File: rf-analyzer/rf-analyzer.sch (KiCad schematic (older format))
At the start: 57 parts, among them U1 AD8302, U2 AD8302

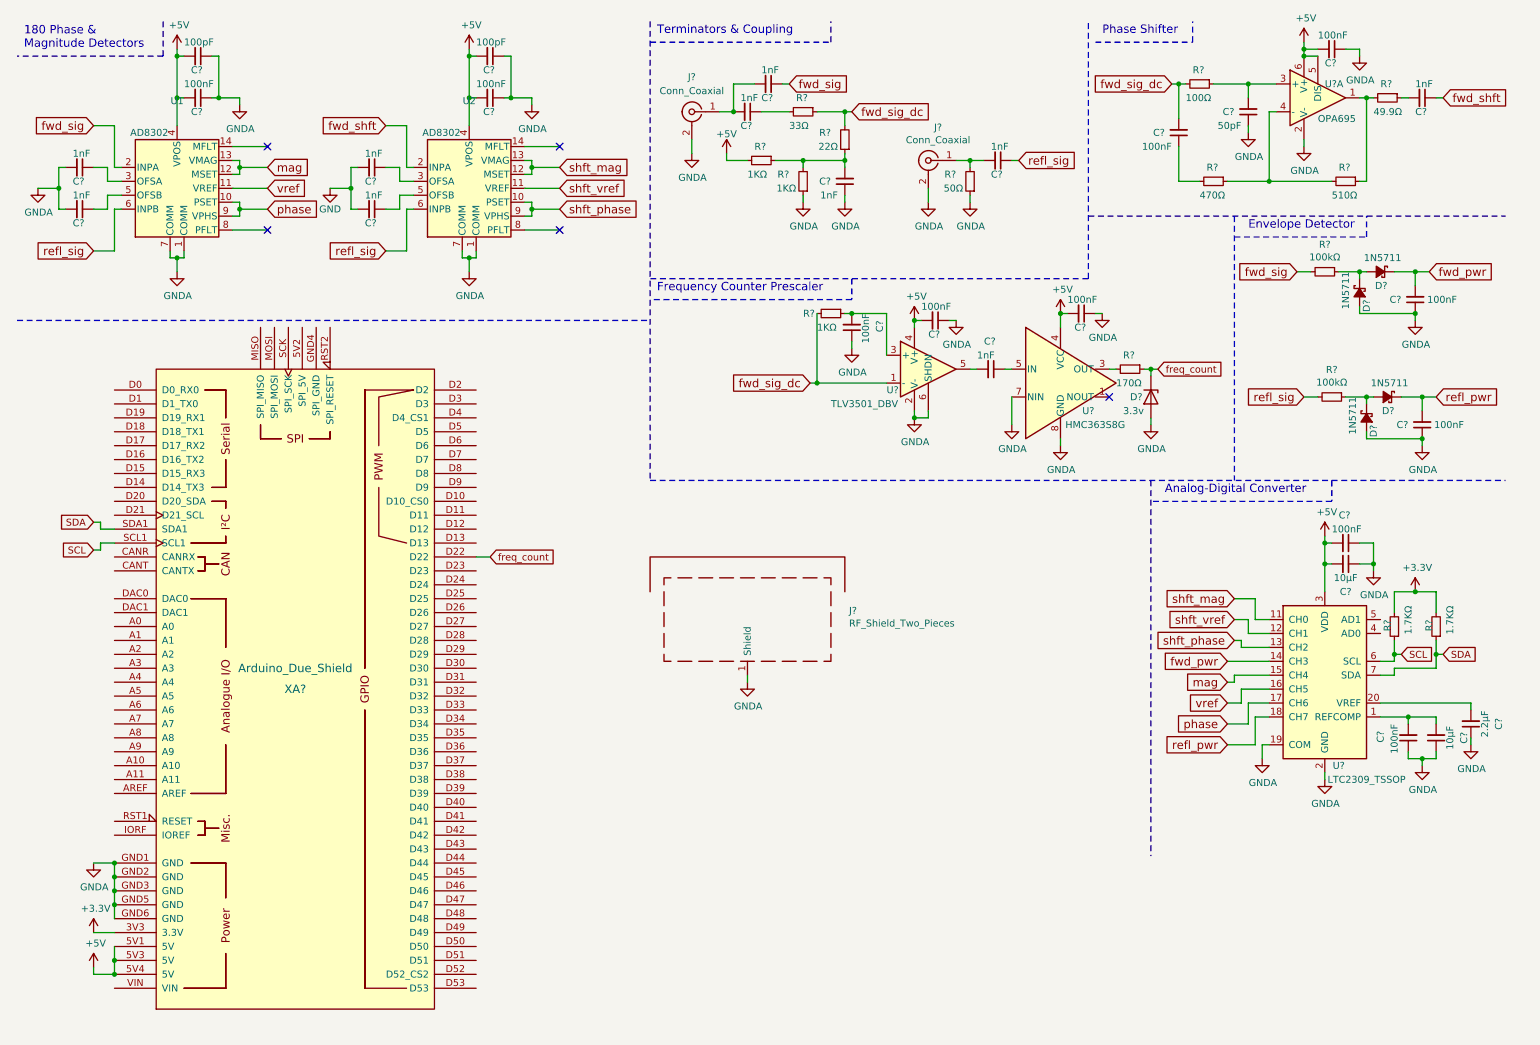
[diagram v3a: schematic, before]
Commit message: moved tank on powerrail to new location.
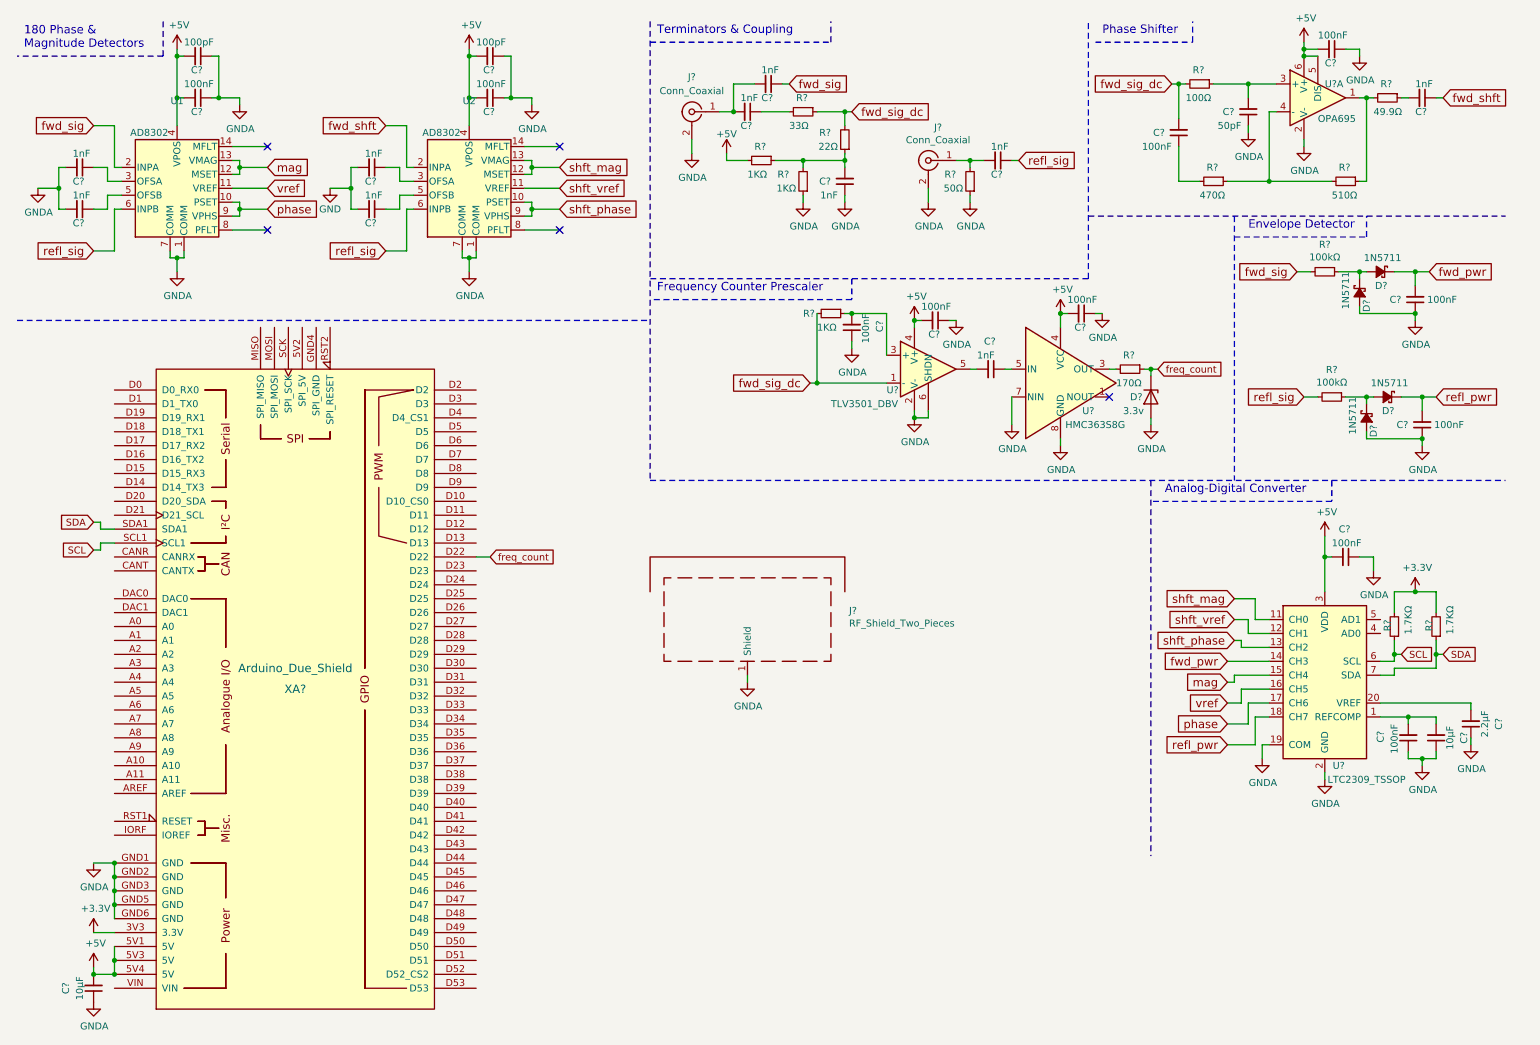
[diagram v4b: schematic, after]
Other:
- moved on the sheet: C?
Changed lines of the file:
@@
 L Device:C_Small C?
 U 1 1 5C8820EC
-P 10050 4250
-F 0 "C?" V 9850 4200 50  0000 L CNN
-F 1 "100nF" V 9950 4150 50  0000 L CNN
-F 2 "Capacitor_SMD:C_0603_1608Metric_Pad1.05x0.95mm_HandSolder" H 10050 4250 50  0001 C CNN
-F 3 "" H 10050 4250 50  0001 C CNN
-	1    10050 4250
+P 10050 4350
+F 0 "C?" V 9850 4300 50  0000 L CNN
+F 1 "100nF" V 9950 4250 50  0000 L CNN
+F 2 "Capacitor_SMD:C_0603_1608Metric_Pad1.05x0.95mm_HandSolder" H 10050 4350 50  0001 C CNN
+F 3 "" H 10050 4350 50  0001 C CNN
+	1    10050 4350
 	0    1    1    0
 $EndComp
@@
 L Device:C_Small C?
 U 1 1 5C882A0E
-P 10050 4400
-F 0 "C?" V 10250 4400 50  0000 C CNN
-F 1 "10μF" V 10150 4400 50  0000 C CNN
-F 2 "" H 10050 4400 50  0001 C CNN
-F 3 "~" H 10050 4400 50  0001 C CNN
-	1    10050 4400
-	0    1    1    0
+P 1050 7450
+F 0 "C?" V 1250 7450 50  0000 C CNN
+F 1 "10μF" V 1150 7450 50  0000 C CNN
+F 2 "" H 1050 7450 50  0001 C CNN
+F 3 "~" H 1050 7450 50  0001 C CNN
+	1    1050 7450
+	-1   0    0    1
 $EndComp
 $Comp
@@
 $EndComp
 Wire Wire Line
-	9900 4600 9900 4400
-Wire Wire Line
-	9900 4250 9950 4250
-Wire Wire Line
-	9950 4400 9900 4400
-Connection ~ 9900 4400
-Wire Wire Line
-	9900 4400 9900 4250
-Wire Wire Line
-	10250 4450 10250 4400
-Wire Wire Line
-	10250 4250 10150 4250
-Wire Wire Line
-	10150 4400 10250 4400
-Connection ~ 10250 4400
-Wire Wire Line
-	10250 4400 10250 4250
+	9900 4350 9950 4350
 $Comp
 L power:+5V #PWR?
@@
 	1    0    0    -1
 $EndComp
-Wire Wire Line
-	9900 4200 9900 4250
-Connection ~ 9900 4250
 $Comp
 L power:GNDA #PWR?
@@
 Wire Wire Line
 	1050 7300 1050 7350
-Wire Wire Line
-	1200 6550 1050 6550
 $Comp
 L arduino:Arduino_Due_Shield XA?
@@
 Wire Notes Line
 	8200 2350 5050 2350
+Wire Wire Line
+	9900 4200 9900 4350
+Connection ~ 9900 4350
+Wire Wire Line
+	9900 4350 9900 4600
+Wire Wire Line
+	10250 4450 10250 4350
+Wire Wire Line
+	10250 4350 10150 4350
+Connection ~ 1050 7350
+Wire Wire Line
+	1050 6550 1200 6550
+$Comp
+L power:GNDA #PWR?
+U 1 1 60478DD4
+P 1050 7550
+F 0 "#PWR?" H 1050 7300 50  0001 C CNN
+F 1 "GNDA" H 1055 7377 50  0000 C CNN
+F 2 "" H 1050 7550 50  0001 C CNN
+F 3 "" H 1050 7550 50  0001 C CNN
+	1    1050 7550
+	1    0    0    -1
+$EndComp
 $EndSCHEMATC

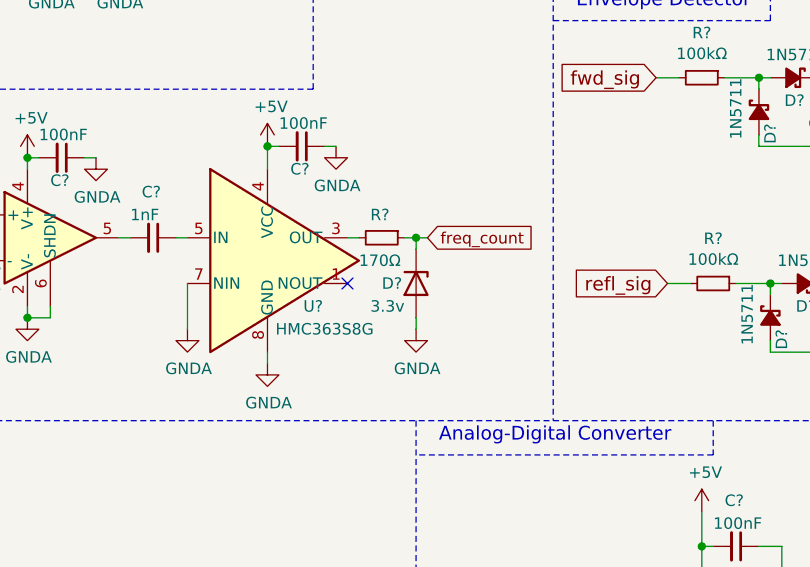
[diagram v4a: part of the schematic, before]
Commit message: Replaced the zener with a voltage divder for better frequency response.
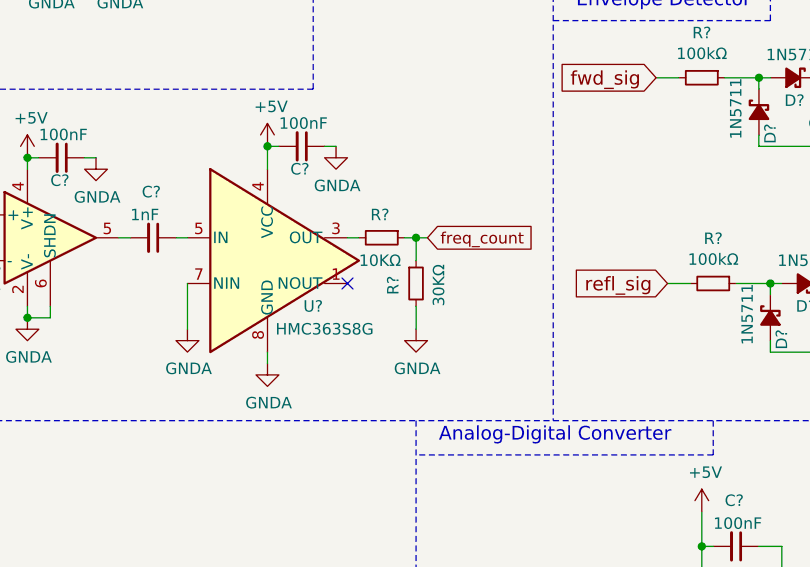
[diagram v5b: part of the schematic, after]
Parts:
- removed D?: 3.3v, symbol Device:D_Zener
- added R?: 30KΩ, Resistor_SMD:R_0603_1608Metric_Pad1.05x0.95mm_HandSolder, symbol Device:R_Small
- R?: value 170Ω -> 10KΩ
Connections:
- net GNDA: now also R?.2
- net freq_count: now also R?.1
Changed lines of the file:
@@
 	6200 3100 6250 3100
-$Comp
-L Device:R_Small R?
-U 1 1 5F77CD96
-P 8500 3000
-F 0 "R?" V 8400 2950 50  0000 L CNN
-F 1 "170Ω" V 8600 2900 50  0000 L CNN
-F 2 "Resistor_SMD:R_0603_1608Metric_Pad1.05x0.95mm_HandSolder" H 8500 3000 50  0001 C CNN
-F 3 "" H 8500 3000 50  0001 C CNN
-	1    8500 3000
-	0    1    1    0
-$EndComp
-$Comp
-L Device:D_Zener D?
-U 1 1 5F7D1F53
-P 8650 3200
-F 0 "D?" V 8650 3050 50  0000 L CNN
-F 1 "3.3v" V 8750 3000 50  0000 L CNN
-F 2 "" H 8650 3200 50  0001 C CNN
-F 3 "~" H 8650 3200 50  0001 C CNN
-	1    8650 3200
-	0    1    1    0
-$EndComp
 $Comp
 L power:GNDA #PWR?
@@
 Wire Wire Line
 	8600 3000 8650 3000
-Wire Wire Line
-	8650 3000 8650 3050
-Wire Wire Line
-	8650 3350 8650 3400
 $Comp
 L power:+5V #PWR?
@@
 	1    0    0    -1
 $EndComp
+$Comp
+L Device:R_Small R?
+U 1 1 5F77CD96
+P 8500 3000
+F 0 "R?" V 8400 2950 50  0000 L CNN
+F 1 "10KΩ" V 8600 2900 50  0000 L CNN
+F 2 "Resistor_SMD:R_0603_1608Metric_Pad1.05x0.95mm_HandSolder" H 8500 3000 50  0001 C CNN
+F 3 "" H 8500 3000 50  0001 C CNN
+	1    8500 3000
+	0    1    1    0
+$EndComp
+$Comp
+L Device:R_Small R?
+U 1 1 604D1349
+P 8650 3200
+F 0 "R?" V 8550 3150 50  0000 L CNN
+F 1 "30KΩ" V 8750 3100 50  0000 L CNN
+F 2 "Resistor_SMD:R_0603_1608Metric_Pad1.05x0.95mm_HandSolder" H 8650 3200 50  0001 C CNN
+F 3 "" H 8650 3200 50  0001 C CNN
+	1    8650 3200
+	1    0    0    -1
+$EndComp
+Wire Wire Line
+	8650 3000 8650 3100
+Wire Wire Line
+	8650 3300 8650 3400
 $EndSCHEMATC

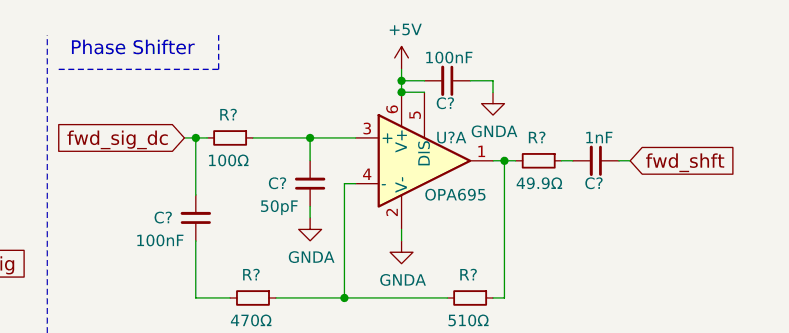
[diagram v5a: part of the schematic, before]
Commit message: moved around a power rail that was outside of the border.
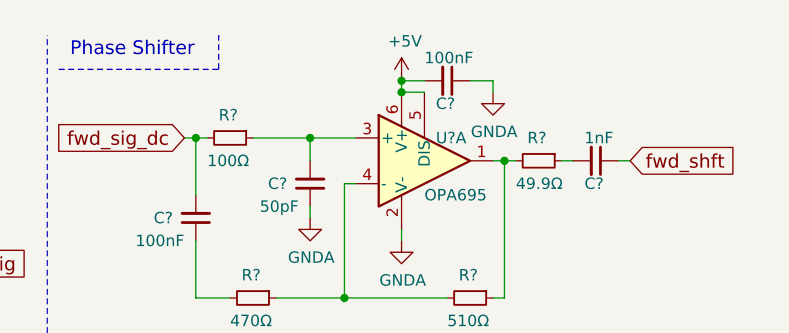
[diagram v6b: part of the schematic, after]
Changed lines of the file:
@@
 fwd_sig
 Wire Wire Line
-	9750 650  9750 700
-Wire Wire Line
 	9850 750  9750 750
-Wire Wire Line
-	9850 700  9750 700
-Connection ~ 9750 700
 Wire Wire Line
 	10050 700  10150 700
@@
 	9400 5700 9200 5700
 Wire Wire Line
-	9750 700  9750 750
-Wire Wire Line
 	9500 1650 9950 1650
 Wire Wire Line
@@
 L power:+5V #PWR0105
 U 1 1 5C5E9076
-P 9750 650
-F 0 "#PWR0105" H 9750 500 50  0001 C CNN
-F 1 "+5V" H 9765 823 50  0000 C CNN
-F 2 "" H 9750 650 50  0001 C CNN
-F 3 "" H 9750 650 50  0001 C CNN
-	1    9750 650
+P 9750 700
+F 0 "#PWR0105" H 9750 550 50  0001 C CNN
+F 1 "+5V" H 9765 873 50  0000 C CNN
+F 2 "" H 9750 700 50  0001 C CNN
+F 3 "" H 9750 700 50  0001 C CNN
+	1    9750 700
 	1    0    0    -1
 $EndComp
@@
 Wire Notes Line
 	9950 3950 8650 3950
-Connection ~ 9750 750
 $Comp
 L power:GNDA #PWR?
@@
 Wire Wire Line
 	8650 3300 8650 3400
+Wire Wire Line
+	9850 700  9750 700
+Wire Wire Line
+	9750 700  9750 750
+Connection ~ 9750 700
+Connection ~ 9750 750
 $EndSCHEMATC

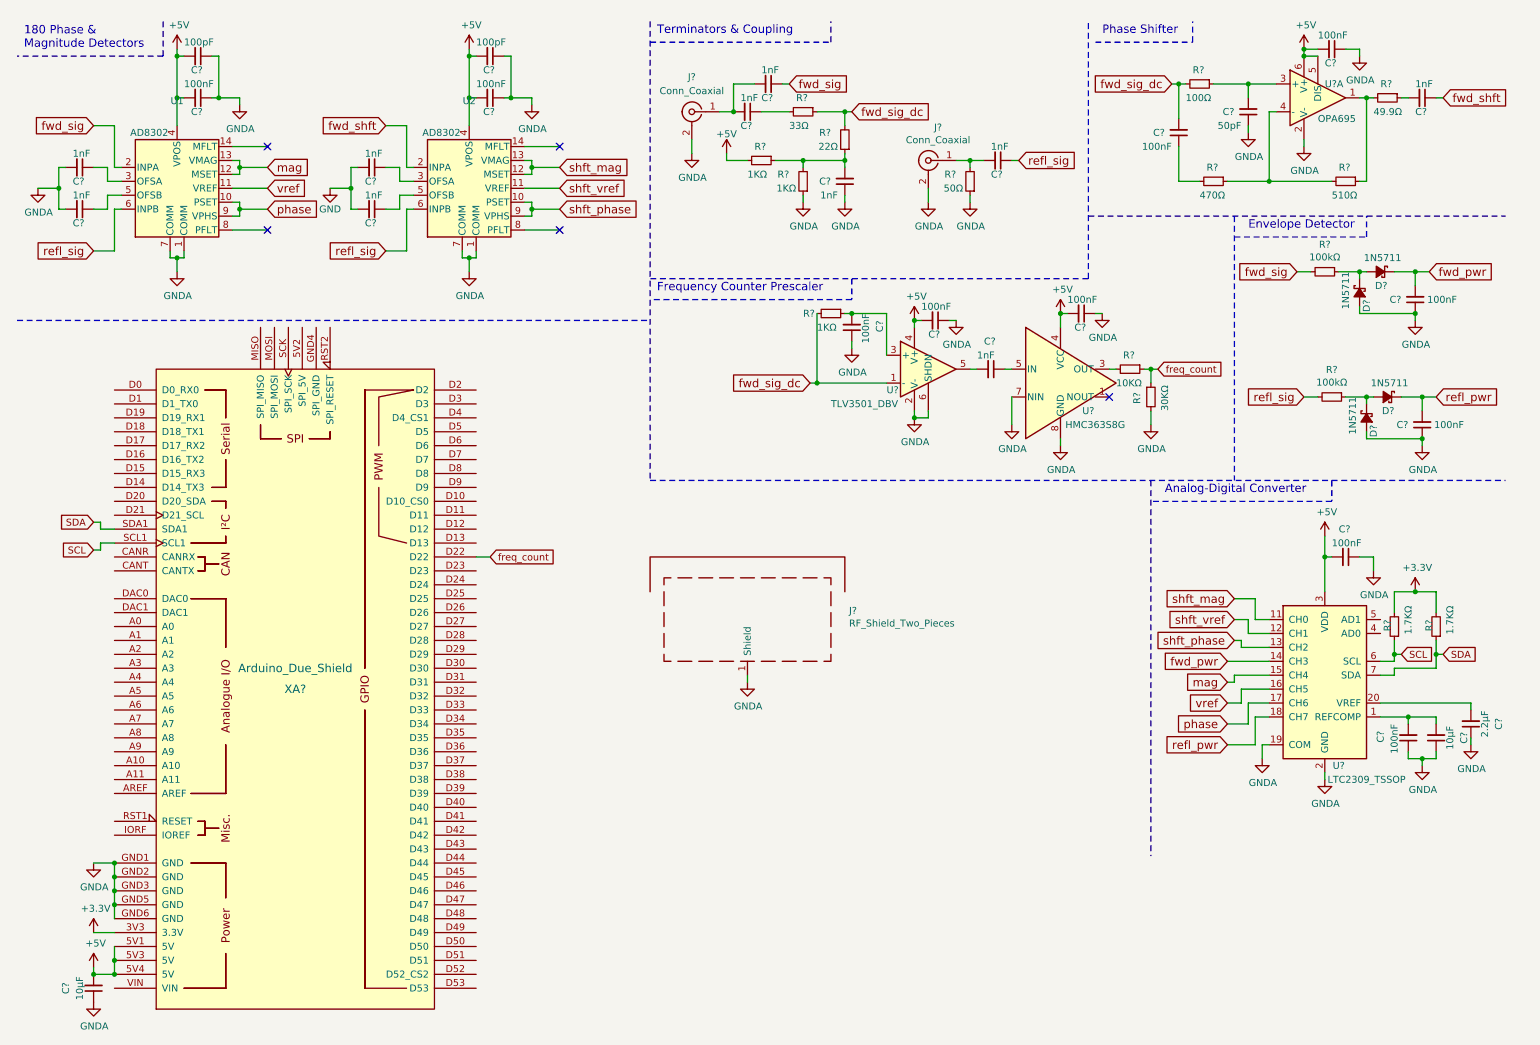
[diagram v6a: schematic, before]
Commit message: Updated footprints in schematic to match new minarturized design.
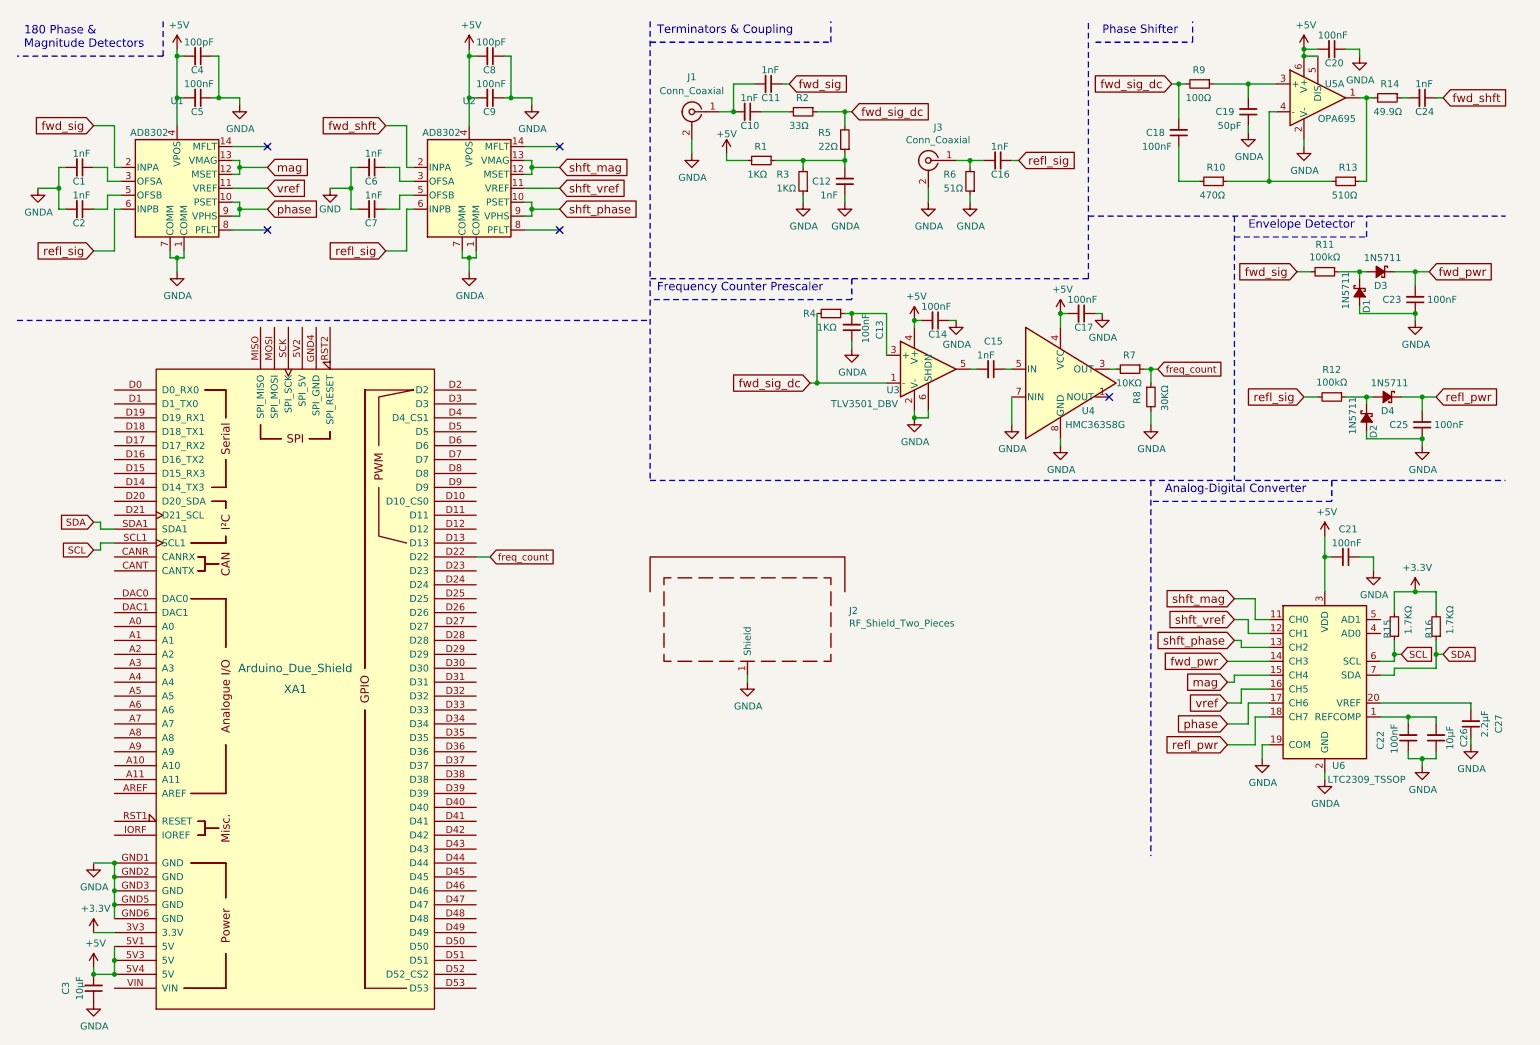
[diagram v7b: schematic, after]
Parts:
- C1, C10, C11, C12, C13, C14, C15, C16, C17, C18, C19, C2, C20, C21, C22, C23, C24, C25, C4, C5, C6, C7, C8, C9: renamed from C?; footprint Capacitor_SMD:C_0603_1608Metric_Pad1.05x0.95mm_HandSolder -> Capacitor_SMD:C_0402_1005Metric
- C26, C3: renamed from C?; footprint (none) -> Capacitor_SMD:C_0603_1608Metric
- C27: renamed from C?; footprint (none) -> Capacitor_SMD:C_0402_1005Metric
- D1, D2, D3, D4: renamed from D?; footprint Diode_SMD:D_SMA -> Diode_SMD:D_SOD-323
- J1, J3: renamed from J?; footprint Connector_Coaxial:U.FL_Molex_MCRF_73412-0110_Vertical -> Connector_Coaxial:SMA_Samtec_SMA-J-P-X-ST-EM1_EdgeMount
- R1, R10, R11, R12, R13, R14, R15, R16, R2, R3, R4, R5, R7, R8, R9: renamed from R?; footprint Resistor_SMD:R_0603_1608Metric_Pad1.05x0.95mm_HandSolder -> Capacitor_SMD:C_0402_1005Metric
- R6: renamed from R?; value 50Ω -> 51Ω; footprint Resistor_SMD:R_0603_1608Metric_Pad1.05x0.95mm_HandSolder -> Capacitor_SMD:C_0402_1005Metric
- gave numbers to parts that had none: 6

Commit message: Becgan populating the PCB.
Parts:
- R14: value 49.9Ω -> 51Ω
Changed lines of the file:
@@
 P 10350 1050
 F 0 "R14" V 10250 1000 50  0000 L CNN
-F 1 "49.9Ω" V 10450 950 50  0000 L CNN
+F 1 "51Ω" V 10450 950 50  0000 L CNN
 F 2 "Capacitor_SMD:C_0402_1005Metric" H 10350 1050 50  0001 C CNN
 F 3 "" H 10350 1050 50  0001 C CNN
